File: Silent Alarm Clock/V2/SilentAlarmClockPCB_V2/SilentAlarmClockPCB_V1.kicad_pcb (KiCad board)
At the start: 4 copper layers, 52 x 31 mm, 28 parts, among them J1 USB_C_Receptacle_USB2.0_16P, J2 Barrel_Jack, J3 B2B-PH-K-S, SW3 RESET, SW4 BOOT, U1 ESD7104MUTAG, U2 ESP32-S3-MINI-1-N8, U3 BQ24040DSQR, U4 TLV75801PDRV

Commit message: V2 preliminary layout
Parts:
- removed D3: LED, LED_SMD:LED_0603_1608Metric
- removed R1: 1k, Resistor_SMD:R_0603_1608Metric
- added C1: 10uF, Capacitor_SMD:C_0603_1608Metric, F.Cu at (170.4, 76.3)
- added C11: 1uF, Capacitor_SMD:C_0603_1608Metric, F.Cu at (178.7, 81.0)
- added C12: 0.1uF, Capacitor_SMD:C_0603_1608Metric, F.Cu at (149.7, 72.5)
- added C13: 0.1uF, Capacitor_SMD:C_0603_1608Metric, F.Cu at (148.7, 79.5)
- added L1: 2.2uH, Inductor_SMD:L_1008_2520Metric, F.Cu at (142.0, 70.6)
- added R10: 100k, Resistor_SMD:R_0603_1608Metric, F.Cu at (172.7, 77.0)
- added R11: 0.01, Resistor_SMD:R_0603_1608Metric, F.Cu at (187.2, 69.0)
- added R12: 4.7k, Resistor_SMD:R_0603_1608Metric, F.Cu at (155.3, 82.0)
- added R13: 4.7k, Resistor_SMD:R_0603_1608Metric, F.Cu at (155.3, 75.5)
- added R14: 10k, Resistor_SMD:R_0603_1608Metric, F.Cu at (155.3, 78.0)
- added R15: 10k, Resistor_SMD:R_0603_1608Metric, F.Cu at (173.2, 73.0)
- added R16: 10k, Resistor_SMD:R_0603_1608Metric, F.Cu at (143.2, 76.5)
- added R17: 10k, Resistor_SMD:R_0603_1608Metric, F.Cu at (185.5, 80.0)
- added R18: 10k, Resistor_SMD:R_0603_1608Metric, F.Cu at (187.2, 75.0)
- added R19: 10k, Resistor_SMD:R_0603_1608Metric, F.Cu at (147.2, 69.0)
- added R8: 180, Resistor_SMD:R_0603_1608Metric, F.Cu at (160.2, 73.0)
- added R9: 1k, Resistor_SMD:R_0603_1608Metric, F.Cu at (165.2, 71.0)
- added SW1: SW_SPDT, Button_Switch_SMD:SW_SPDT_CK_JS102011SAQN, F.Cu at (204.5, 129.9)
- added SW2: RotaryEncoder_Switch, PEC11R_4220F_S0024:XDCR_PEC11R-4220F-S0024, F.Cu at (199.0, 73.0)
- added U5: BQ27441DRZT-G1A, BQ27441DRZT-G1A:Copy of DRZ0012A, F.Cu at (182.0, 68.8)
- C10, C9: value 0.1uF -> 1uF
- C3: value 1uF -> 10uF
- C5: value 1uF -> 0.47uF
- C6, C7, C8: value C -> 1uF
- D1: footprint LED_SMD:LED_0603_1608Metric -> LED_SMD:LED_0603_1608Metric_Pad1.05x0.95mm_HandSolder
- J2: value Barrel_Jack -> B2B-PH-K-S; footprint Connector_BarrelJack:BarrelJack_CLIFF_FC681465S_SMT_Horizontal -> B2B-PH-K-S:JST_B2B-PH-K-S
- J3: value B2B-PH-K-S -> Conn_01x08_Socket; footprint B2B_PH_K_S:JST_B2B-PH-K-S -> Connector_JST:JST_PH_B8B-PH-K_1x08_P2.00mm_Vertical
- R2, R3: value R -> 5.1k
- R4: value 540 -> 100k
- R5: value 1k -> 10k
- R6: value 1k -> 590
- R7: value 1k -> 440
- U1: value ESD7104MUTAG -> BQ24075TRGTR; footprint ESD7104MUTAG:UDFN10_ONS -> BQ24075TRGTR:RGT16_1P7X1P7
- U3: value BQ24040DSQR -> TPS63001; footprint BQ24040DSQR:SON40P200X200X80-11N -> Package_SON:Texas_DRC0010J_ThermalVias
- U4: value TLV75801PDRV -> ESD7104MUTAG; footprint Package_SON:WSON-6-1EP_2x2mm_P0.65mm_EP1x1.6mm -> ESD7104MUTAG:UDFN10_ONS
- moved J2 179.2 mm to (201.4, 103.5), turned to 90 degrees
- moved R4 172.9 mm to (195.7, 132.5)
- moved C2 162.5 mm to (193.2, 104.0), turned to 0 degrees
- moved SW4 145.8 mm to (201.6, 95.2)
- moved U1 144.0 mm to (182.0, 75.0), turned to 0 degrees
- moved SW3 133.9 mm to (201.6, 90.4)
- moved C5 132.6 mm to (177.0, 68.5)
- moved C4 128.7 mm to (177.0, 66.0), turned to 0 degrees
- moved C10 122.4 mm to (178.7, 78.5), turned to 0 degrees
- moved R5 122.2 mm to (173.7, 69.0), turned to 0 degrees
- moved C3 119.3 mm to (133.3, 125.5)
- moved D1 118.1 mm to (170.4, 68.0), turned to 0 degrees
- moved J1 117.3 mm to (119.0, 129.5)
- moved D2 115.3 mm to (169.8, 71.5), turned to 0 degrees
- moved R2 115.2 mm to (127.5, 124.5), turned to 0 degrees
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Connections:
- C10 pad 1: Net-(U2-IO0) -> GND
- C10 pad 2: GND -> Encoder_A
- C2 pad 1: /5VIN -> BATTERY_IN
- C3 pad 1: Net-(U3-OUT) -> V_USB
- C4 pad 1: Net-(U3-OUT) -> GND
- C4 pad 2: GND -> BATTERY_IN
- C5 pad 1: /3V3 -> GND
- C5 pad 2: GND -> 1.8V
- C6 pad 1: /5VIN -> GND
- C6 pad 2: GND -> OUT
- C7 pad 1: /3V3 -> GND
- C7 pad 2: GND -> Net-(U3-EN)
- C8 pad 1: /3V3 -> GND
- C8 pad 2: GND -> 3V3
- C9 pad 1: Net-(U2-EN) -> GND
- C9 pad 2: GND -> 3V3
- D1 pad 2: Net-(D1-A) -> OUT
- D2 pad 2: Net-(D2-A) -> OUT
- J1 pad A4: Net-(J1-VBUS-PadA4) -> V_USB
- J1 pad A5: unconnected-(J1-CC1-PadA5) -> CC1
- J1 pad A6: /USB_P -> D+
- J1 pad A7: /USB_N -> D-
- J1 pad A9: Net-(J1-VBUS-PadA4) -> V_USB
- J1 pad B4: Net-(J1-VBUS-PadA4) -> V_USB
- J1 pad B5: unconnected-(J1-CC2-PadB5) -> CC2
- J1 pad B6: /USB_P -> D+
- J1 pad B7: /USB_N -> D-
- J1 pad B9: Net-(J1-VBUS-PadA4) -> V_USB
- J1 pad SH: GND -> SHEILD
- J2 pad 1: /5VIN -> GND
- J2 pad 2: GND -> BATTERY_IN
- J3 pad 1: Net-(U3-OUT) -> 3V3
- R2 pad 1: /3V3 -> CC1
- R2 pad 2: Net-(U4-FB) -> GND
- R3 pad 1: Net-(U4-FB) -> CC2
- R4 pad 1: Net-(U3-ISET) -> Net-(SW1-A)
- R4 pad 2: GND -> BATTERY_IN
- R5 pad 1: Net-(U3-OUT) -> GND
- R5 pad 2: Net-(D1-A) -> Net-(U1-TS)
- R6 pad 1: Net-(U3-OUT) -> Net-(U1-ISET)
- R6 pad 2: Net-(D2-A) -> GND
- R7 pad 1: /3V3 -> Net-(U1-ILIM)
- R7 pad 2: Net-(D3-A) -> GND
- U1 pad 1: /USB_P -> Net-(U1-TS)
- U1 pad 10: unconnected-(U1-NC-Pad10) -> OUT
- U1 pad 2: /USB_N -> BATTERY_IN
- U1 pad 3: GND -> BATTERY_IN
- U1 pad 4: /5VIN -> Net-(U1-*CE)
- U1 pad 5: unconnected-(U1-I/O-Pad5) -> GND
- U1 pad 6: unconnected-(U1-NC-Pad6) -> Net-(U1-EN1)
- U1 pad 7: unconnected-(U1-NC-Pad7) -> PGOOD
- U1 pad 9: unconnected-(U1-NC-Pad9) -> Net-(U1-*CHG)
- U2 pad 12: unconnected-(U2-IO8-Pad12) -> SDA
- U2 pad 13: unconnected-(U2-IO9-Pad13) -> SCL
- U2 pad 14: unconnected-(U2-IO10-Pad14) -> CS
- U2 pad 15: unconnected-(U2-IO11-Pad15) -> DIN
- U2 pad 16: unconnected-(U2-IO12-Pad16) -> CLK
- U2 pad 17: unconnected-(U2-IO13-Pad17) -> D/C
- U2 pad 18: unconnected-(U2-IO14-Pad18) -> RST
- U2 pad 19: unconnected-(U2-IO15-Pad19) -> BUSY
- U2 pad 23: /USB_N -> D-
- U2 pad 24: /USB_P -> D+
- U2 pad 25: unconnected-(U2-IO21-Pad25) -> S1
- U2 pad 28: unconnected-(U2-IO33-Pad28) -> Encoder_A
- U2 pad 29: unconnected-(U2-IO34-Pad29) -> Encoder_B
- U2 pad 3: /3V3 -> 3V3
- U3 pad 1: /5VIN -> 3V3
- U3 pad 10: Net-(U3-OUT) -> 3V3
- U3 pad 2: Net-(U3-ISET) -> Net-(U3-L2)
- U3 pad 4: unconnected-(U3-PRETERM-Pad4) -> Net-(U3-L1)
- U3 pad 5: Net-(D1-K) -> OUT
- U3 pad 6: (no net) -> Net-(U3-EN)
- U3 pad 7: GND -> Net-(U3-EN)
- U3 pad 8: Net-(D2-K) -> Net-(U3-EN)
- U3 pad 9: unconnected-(U3-TS-Pad9) -> GND
- U4 pad 1: /3V3 -> D-
- U4 pad 2: Net-(U4-FB) -> D+
- U4 pad 4: Net-(U3-OUT) -> V_USB
- U4 pad 6: Net-(U3-OUT) -> unconnected-(U4-NC-Pad6)
- U4 pad 7: GND -> unconnected-(U4-NC-Pad7)
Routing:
- net /3V3: track 78.3 -> 0.00 mm, vias 2 -> 0
- net GND: track 58.2 -> 0.00 mm, vias 68 -> 0
- net Net-(U3-OUT): track 41.5 -> 0.00 mm
- net /5VIN: track 40.1 -> 0.00 mm, vias 10 -> 0
- net /USB_N: track 37.1 -> 0.00 mm
- net /USB_P: track 36.7 -> 0.00 mm
- net Net-(U2-EN): track 18.8 -> 0.00 mm
- net Net-(D2-K): track 12.1 -> 0.00 mm
- net Net-(U2-IO0): track 11.1 -> 0.00 mm
- net Net-(D1-K): track 9.88 -> 0.00 mm
- net Net-(J1-VBUS-PadA4): track 6.21 -> 0.00 mm
- net Net-(U4-FB): track 4.86 -> 0.00 mm
- net Net-(U3-ISET): track 4.54 -> 0.00 mm
- net Net-(D3-A): track 1.67 -> 0.00 mm
- net Net-(D2-A): track 1.67 -> 0.00 mm
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- removed copper zone on In2.Cu, net /5VIN
- removed copper zone on B.Cu, net GND
- removed copper zone on F.Cu, net GND
- removed copper zone on In1.Cu, net GND
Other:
- board size 52 x 31 mm -> 92.5 x 68.4 mm

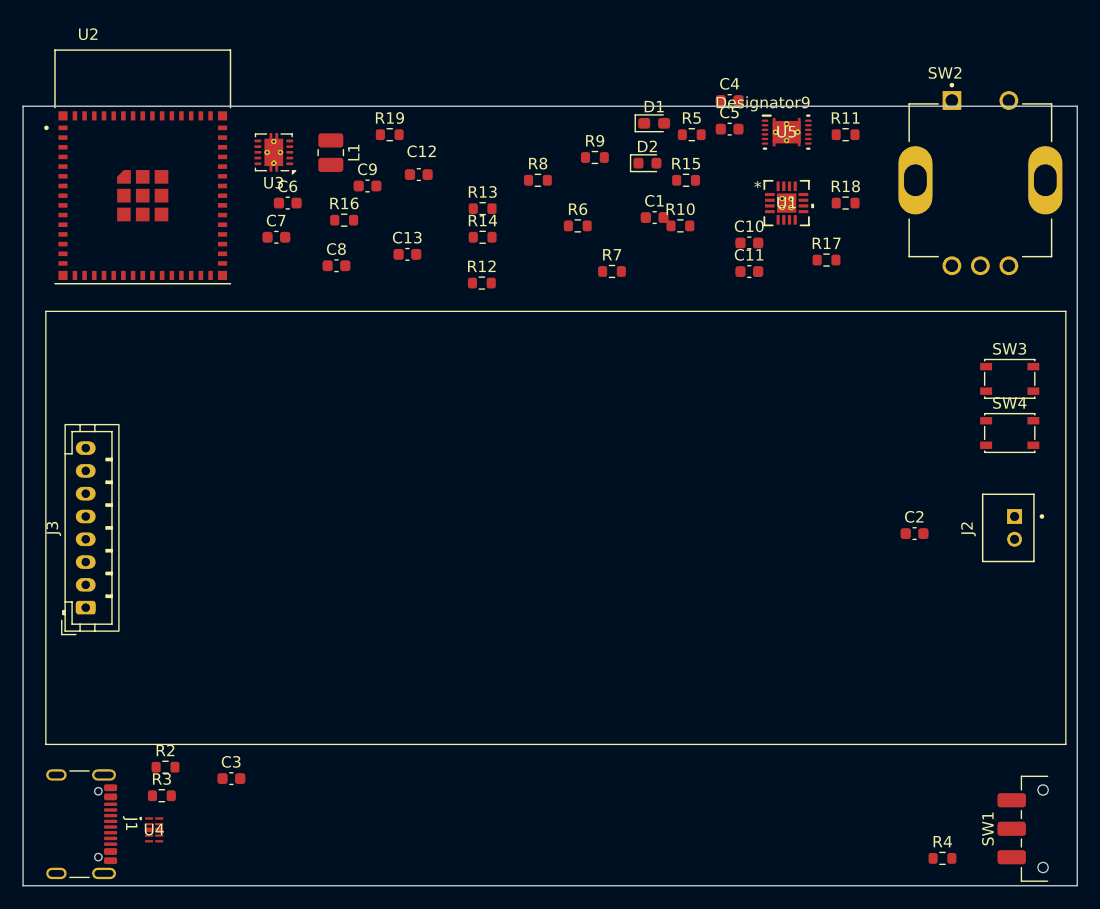
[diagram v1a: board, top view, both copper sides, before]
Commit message: V2 most non pwr traces added
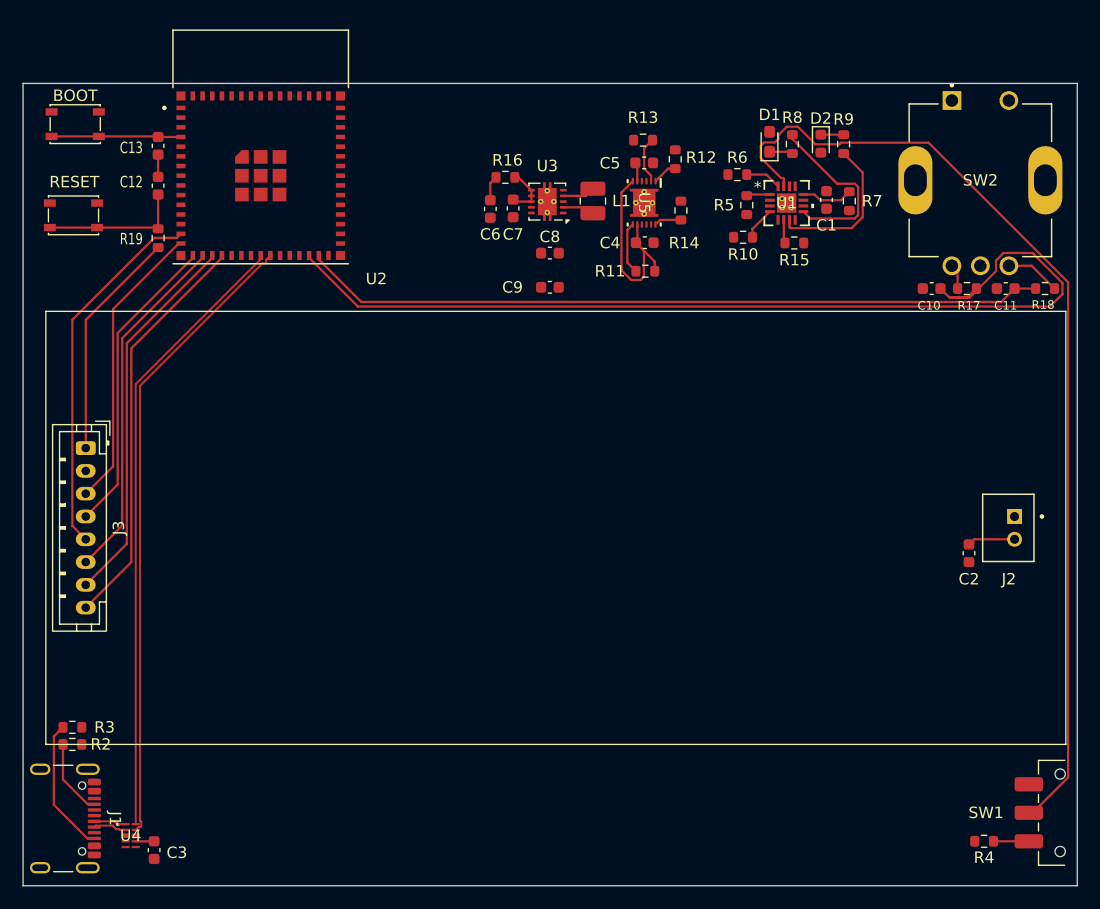
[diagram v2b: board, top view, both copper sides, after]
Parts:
- moved BOOT 86.4 mm to (119.6, 68.1)
- moved RESET 83.4 mm to (119.4, 76.1)
- moved U3 24.4 mm to (161.0, 74.9)
- moved C13 23.9 mm to (126.8, 70.0), turned to 90 degrees
- moved L1 23.4 mm to (165.0, 74.8)
- moved C12 22.9 mm to (126.8, 73.5), turned to -90 degrees
- moved R8 22.5 mm to (182.5, 69.8), turned to 90 degrees
- moved C11 22.5 mm to (201.2, 82.5)
- moved R19 22.3 mm to (126.8, 78.1), turned to 90 degrees
- moved R9 21.9 mm to (187.0, 69.8), turned to -90 degrees
- moved R7 21.7 mm to (187.5, 74.8), turned to -90 degrees
- moved R11 21.3 mm to (169.6, 81.0), turned to 180 degrees
- moved C7 20.9 mm to (158.0, 75.5), turned to 90 degrees
- moved R12 20.2 mm to (172.2, 71.1), turned to -90 degrees
- moved R18 19.0 mm to (204.7, 82.5), turned to 180 degrees
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- renumbered SW4 to BOOT, SW3 to RESET
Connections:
- U4 pad 10: unconnected-(U4-NC-Pad10) -> D-
- U4 pad 7: unconnected-(U4-NC-Pad7) -> V_USB
- U4 pad 9: unconnected-(U4-NC-Pad9) -> D+
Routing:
- net Encoder_A: track 0.00 -> 86.5 mm
- net SYSOFF: track 0.00 -> 86.3 mm
- net Encoder_B: track 0.00 -> 65.3 mm
- net D+: track 0.00 -> 58.7 mm
- net D-: track 0.00 -> 57.3 mm
- net BUSY: track 0.00 -> 35.8 mm
- net RST: track 0.00 -> 33.5 mm
- net CS: track 0.00 -> 32.4 mm
- net D/C: track 0.00 -> 31.1 mm
- net CLK: track 0.00 -> 26.8 mm
- net DIN: track 0.00 -> 25.5 mm
- net BATTERY_IN: track 0.00 -> 23.0 mm
- net 3V3: track 0.00 -> 20.2 mm
- net Net-(U1-*CHG): track 0.00 -> 15.5 mm
- net PGOOD: track 0.00 -> 13.8 mm
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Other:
- board size 92.5 x 68.4 mm -> 92.5 x 70.4 mm

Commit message: V2 layout finished
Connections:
- U5 pad 3: GND -> (no net)
- U5 pad V: (no net) -> GND
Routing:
- net GND: track 0.00 -> 97.0 mm, vias 0 -> 32
- net SCL: track 4.15 -> 64.6 mm, vias 0 -> 2
- net SDA: track 2.18 -> 58.4 mm, vias 0 -> 2
- net BATTERY_IN: track 23.0 -> 63.8 mm, vias 0 -> 6
- net Net-(U2-EN): track 12.5 -> 38.9 mm, vias 0 -> 2
- net 3V3: track 20.2 -> 39.9 mm, vias 0 -> 13
- net OUT: track 2.21 -> 14.5 mm, vias 0 -> 7
- net V_USB: track 1.62 -> 9.70 mm, vias 0 -> 5
- added copper zone on In2.Cu, net 3V3
- added copper zone on In1.Cu, net BATTERY_IN
- added copper zone on B.Cu, net GND
- added copper zone on F.Cu, net GND
- added copper zone on In1.Cu, net OUT
- added copper zone on In2.Cu, net V_USB
